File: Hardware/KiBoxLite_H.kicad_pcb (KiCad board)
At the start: 4 copper layers, 48.8 x 86.8 mm, 163 parts, among them J1 Screw_Terminal_01x03, J2 USB4105-GF-A-060, Q2 BC817-40(SOT23), Q3 BC817-40(SOT23), T1 LMUN2211LT1G(SOT-23), U1 CH340X(MSOP-10), U10 MAX13487, U3 TP4054-42-SOT25-R(SOT23-5), U4 LAN8710A-EZC(QFN32), U5 TX4138(ESOIC-8)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

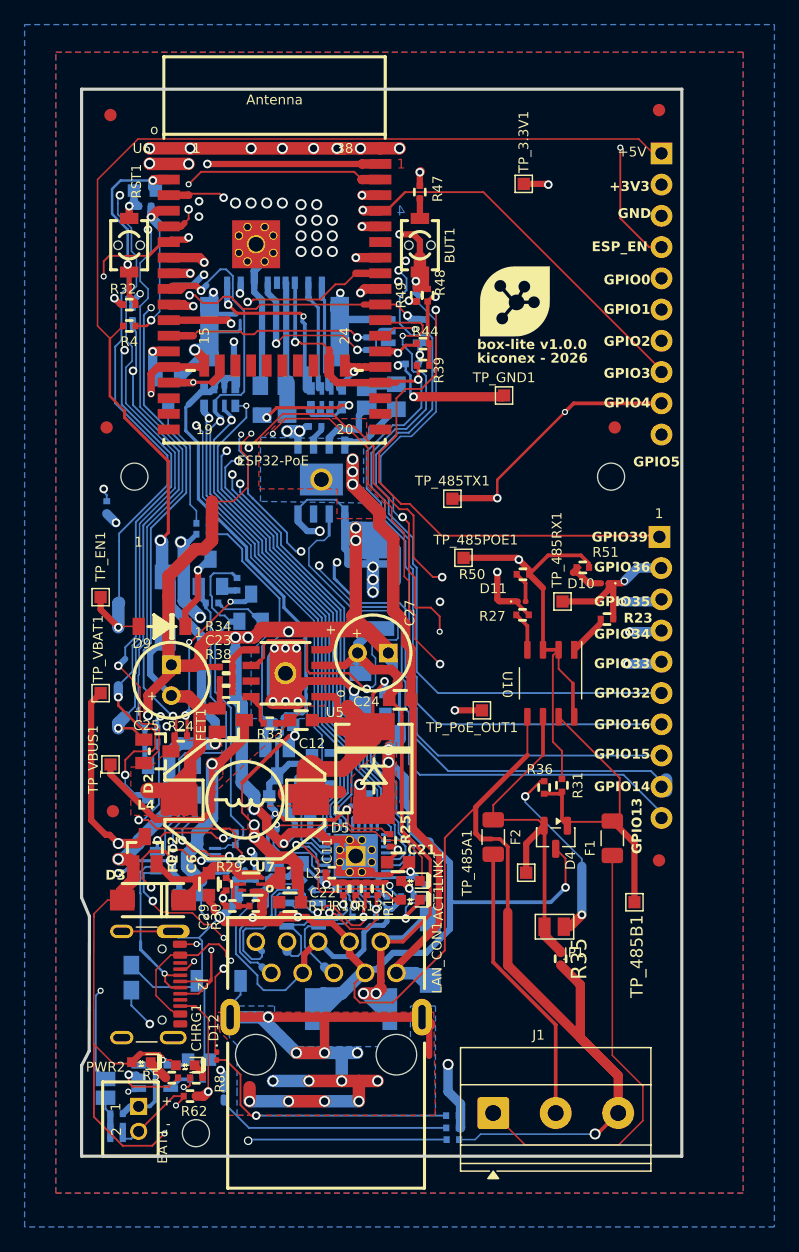
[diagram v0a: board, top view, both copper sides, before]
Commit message: build: fuse ts250
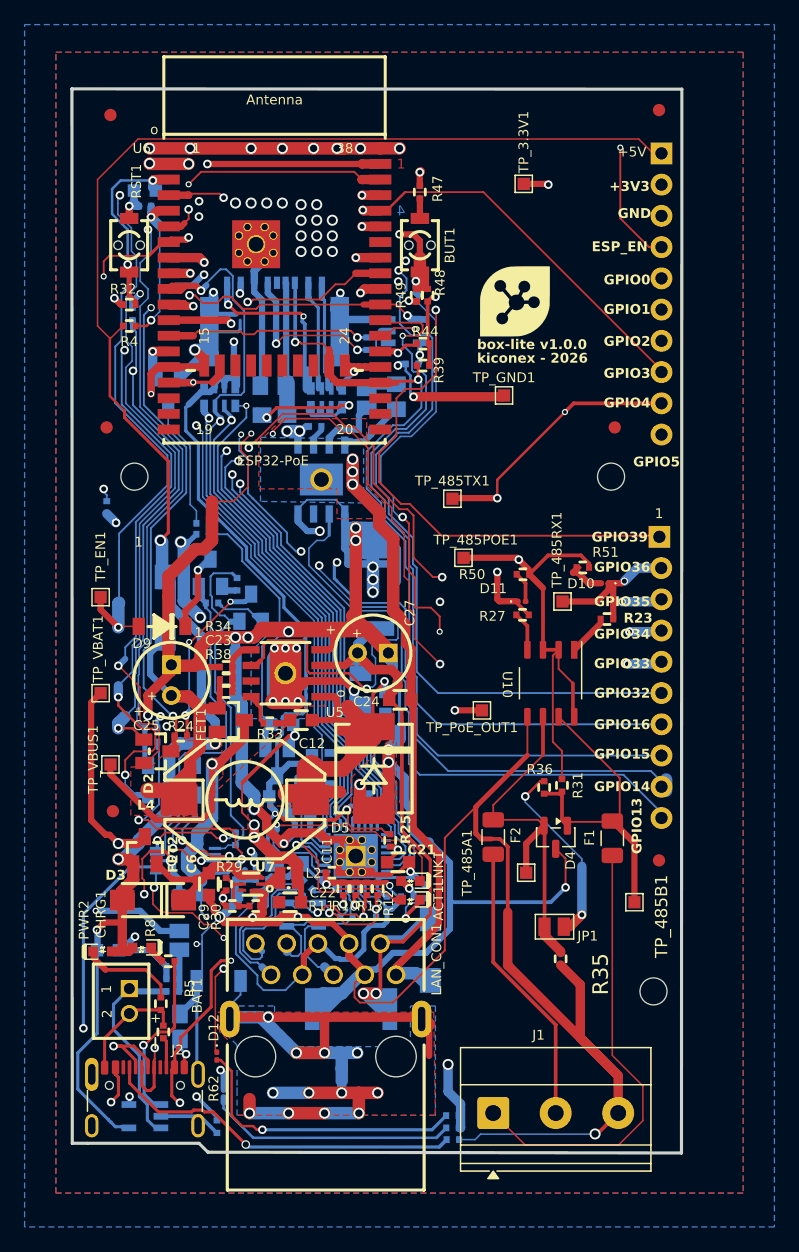
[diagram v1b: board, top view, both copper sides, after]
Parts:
- moved MH3 38.9 mm to (134.9, 159.8)
- moved C19 14.7 mm to (95.9, 157.8), turned to 180 degrees
- moved BAT_SENS_E1 13.4 mm to (96.4, 155.7)
- moved R22 12.8 mm to (95.9, 158.8), turned to 180 degrees
- moved C1 11.6 mm to (90.6, 156.5)
- moved R17 10.9 mm to (95.9, 159.8), turned to 0 degrees
- moved J2 10.4 mm to (93.6, 169.7), turned to 0 degrees
- moved CHRG1 10.2 mm to (93.3, 156.3)
- moved R8 9.74 mm to (95.5, 157.4), turned to 0 degrees
- moved BAT1 9.61 mm to (88.8, 160.7)
- moved PWR2 9.54 mm to (90.2, 156.6), turned to 0 degrees
- moved R5 6.08 mm to (94.9, 160.8), turned to -90 degrees
- moved R62 5.65 mm to (95.1, 163.2), turned to 90 degrees
- moved L7 5.60 mm to (96.5, 162.7)
- moved R6 4.19 mm to (99.5, 170.8), turned to -90 degrees
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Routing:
- net GND: track 615.2 -> 589.9 mm, vias 64 -> 62
- net +5V: track 239.8 -> 226.1 mm, vias 7 -> 6
- net VBUS: track 53.0 -> 65.4 mm, vias 3 -> 5
- net /D-: track 14.2 -> 26.5 mm, vias 1 -> 2
- net Net-(J2-CC2): track 9.81 -> 2.47 mm, vias 1 -> 0
- net Net-(U3-CHRGb): track 6.93 -> 14.2 mm, vias 2 -> 1
- net Net-(U3-PROG): track 1.90 -> 8.83 mm, vias 0 -> 2
- net /GPI35: track 146.2 -> 139.4 mm
- net /D+: track 20.0 -> 26.8 mm
- net Net-(PWR2-K): track 1.68 -> 7.94 mm
- net Net-(J2-CC1): track 34.2 -> 29.6 mm, vias 2 -> 1
- net Net-(LAN_CON1-Shield): track 61.5 -> 64.0 mm
- net Net-(D12-A): track 22.1 -> 23.6 mm
- net Net-(D13-A): track 19.4 -> 20.3 mm
- net /TD+: track 26.0 -> 25.0 mm
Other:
- board size 48.8 x 86.8 mm -> 49.6 x 86.5 mm

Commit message: build: fuse ts250 modelo 3d
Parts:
- F1, F2: footprint Fuse:Fuse_1206_3216Metric -> kiboard_shield:TS250; moved to B.Cu
- moved F1 11.8 mm to (126.0, 157.8), turned to 180 degrees
- moved F2 4.64 mm to (126.2, 145.4), turned to 180 degrees
- moved TP_485A1 2.25 mm to (122.3, 150.1)
- moved R31 1.54 mm to (129.1, 143.1)
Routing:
- net GND: track 589.9 -> 541.7 mm
- net Net-(J1-Pin_1): track 36.7 -> 11.7 mm
- net /485_A: track 29.7 -> 39.8 mm, vias 0 -> 1
- net /485_B: track 26.5 -> 35.3 mm, vias 0 -> 1
- net Net-(J1-Pin_2): track 23.1 -> 27.6 mm
- net /GPIO13\I2C-SDA: track 70.1 -> 68.1 mm
- net /GPIO15\HS2_CMD: track 72.7 -> 71.8 mm
- net +5V: track 226.1 -> 226.9 mm
- net /GPIO14\HS2_CLK: track 80.2 -> 79.6 mm

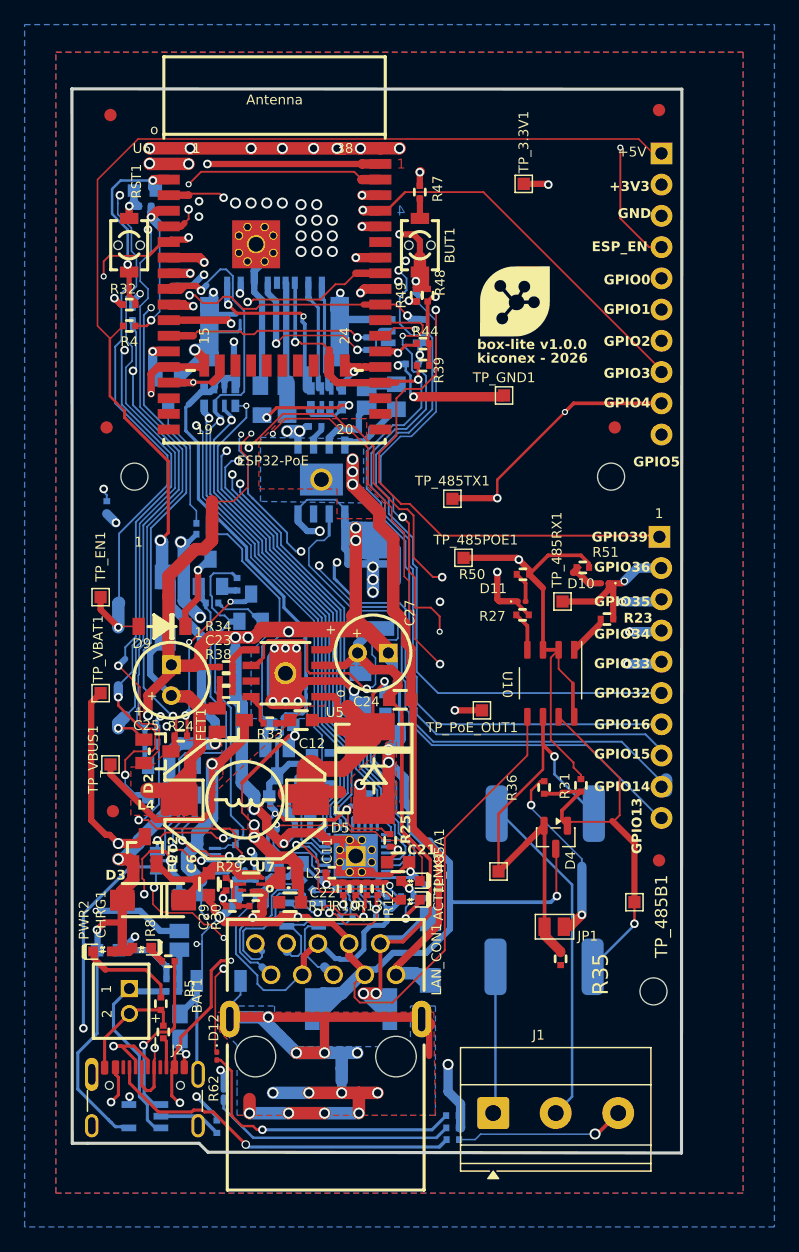
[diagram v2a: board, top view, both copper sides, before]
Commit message: build: Cambio de puerto rs485
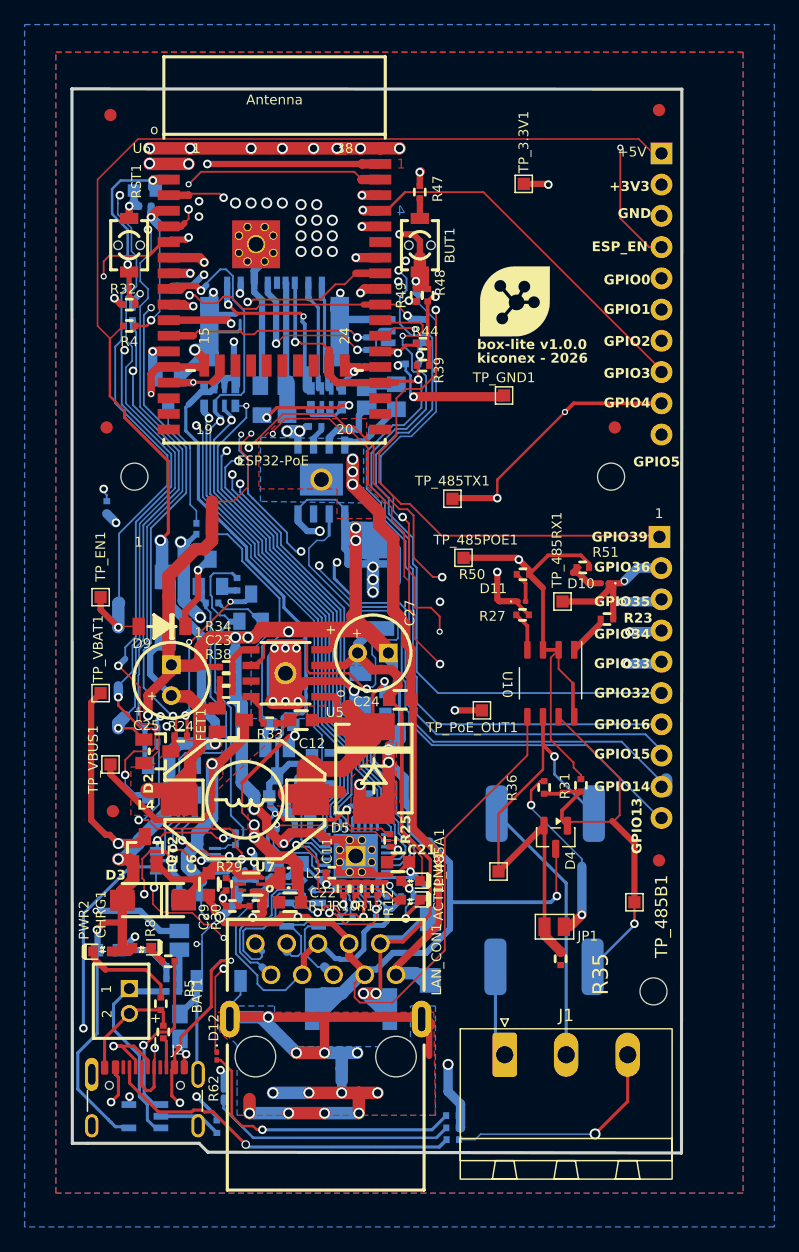
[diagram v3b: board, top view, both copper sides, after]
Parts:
- J1: footprint TerminalBlock_Phoenix:TerminalBlock_Phoenix_MKDS-1,5-3-5.08_1x03_P5.08mm_Horizontal -> Connector_Phoenix_MSTB:PhoenixContact_MSTBA_2,5_3-G_1x03_P5.00mm_Horizontal
- moved J1 4.83 mm to (122.8, 165.0)
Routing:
- net Net-(J1-Pin_2): track 27.6 -> 21.9 mm
- net GND: track 541.7 -> 546.8 mm
- net Net-(J1-Pin_1): track 11.7 -> 7.46 mm
